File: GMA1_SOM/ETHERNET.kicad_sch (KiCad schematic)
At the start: 6 parts, among them U3 LAN8742A-CZ-TR, Y1 SG-210STF 25.0000ML0

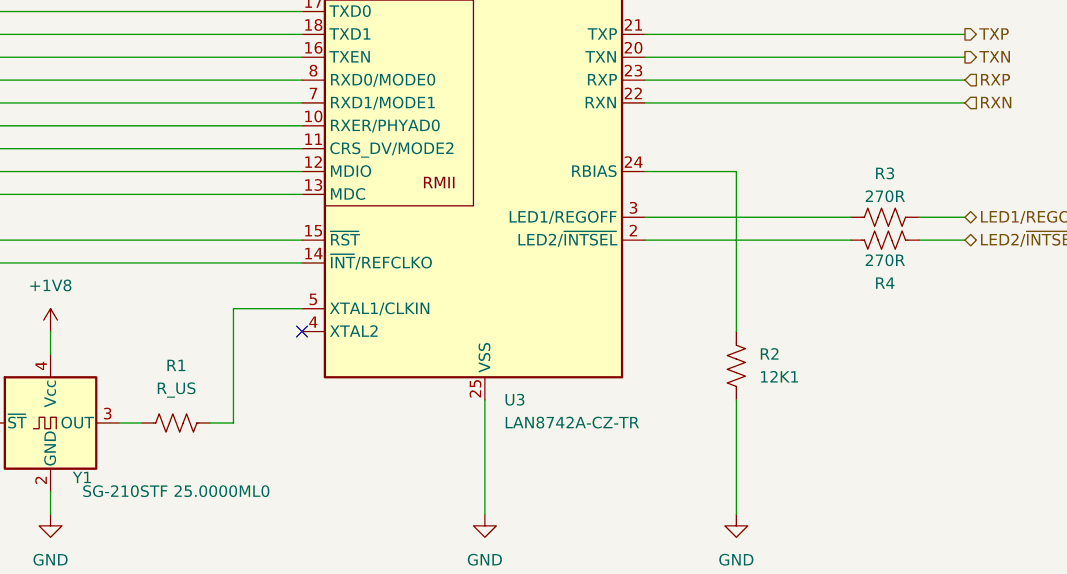
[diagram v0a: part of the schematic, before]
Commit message: add display and ram
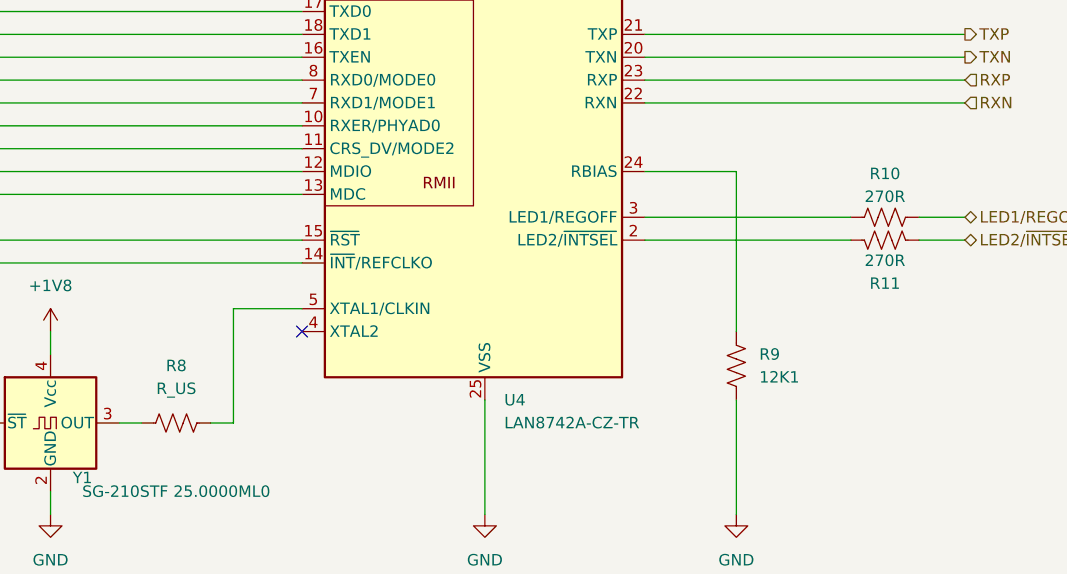
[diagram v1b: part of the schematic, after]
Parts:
- renumbered R3 to R10, R4 to R11, R1 to R8, R2 to R9, U3 to U4
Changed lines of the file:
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@@
 		(on_board yes)
 		(dnp no)
-		(property "Reference" "R3"
+		(property "Reference" "R10"
 			(at 193.04 94.234 90)
 			(effects
@@
 			(project "GMA1_SOM"
 				(path "/d784c6f3-1f62-4397-857c-3a97e2a0cbd1/9d08b115-8d2a-4cae-b926-cec128a135e3/42807cf7-1018-4a17-8e91-245329e48274"
-					(reference "R3")
-					(unit 1)
-				)
-				(path "/d784c6f3-1f62-4397-857c-3a97e2a0cbd1/9d08b115-8d2a-4cae-b926-cec128a135e3/7528c9fa-157b-4a38-85d4-57bc56cff310"
-					(reference "R7")
+					(reference "R10")
+					(unit 1)
+				)
+				(path "/d784c6f3-1f62-4397-857c-3a97e2a0cbd1/9d08b115-8d2a-4cae-b926-cec128a135e3/7528c9fa-157b-4a38-85d4-57bc56cff310"
+					(reference "R14")
 					(unit 1)
 				)
@@
 		(dnp no)
 		(fields_autoplaced yes)
-		(property "Reference" "#PWR05"
+		(property "Reference" "#PWR018"
 			(at 146.05 45.72 0)
 			(effects
@@
 			(project ""
 				(path "/d784c6f3-1f62-4397-857c-3a97e2a0cbd1/9d08b115-8d2a-4cae-b926-cec128a135e3/42807cf7-1018-4a17-8e91-245329e48274"
-					(reference "#PWR05")
-					(unit 1)
-				)
-				(path "/d784c6f3-1f62-4397-857c-3a97e2a0cbd1/9d08b115-8d2a-4cae-b926-cec128a135e3/7528c9fa-157b-4a38-85d4-57bc56cff310"
-					(reference "#PWR013")
+					(reference "#PWR018")
+					(unit 1)
+				)
+				(path "/d784c6f3-1f62-4397-857c-3a97e2a0cbd1/9d08b115-8d2a-4cae-b926-cec128a135e3/7528c9fa-157b-4a38-85d4-57bc56cff310"
+					(reference "#PWR026")
 					(unit 1)
 				)
@@
 		(dnp no)
 		(fields_autoplaced yes)
-		(property "Reference" "#PWR04"
+		(property "Reference" "#PWR017"
 			(at 143.51 39.37 0)
 			(effects
@@
 			(project ""
 				(path "/d784c6f3-1f62-4397-857c-3a97e2a0cbd1/9d08b115-8d2a-4cae-b926-cec128a135e3/42807cf7-1018-4a17-8e91-245329e48274"
-					(reference "#PWR04")
-					(unit 1)
-				)
-				(path "/d784c6f3-1f62-4397-857c-3a97e2a0cbd1/9d08b115-8d2a-4cae-b926-cec128a135e3/7528c9fa-157b-4a38-85d4-57bc56cff310"
-					(reference "#PWR012")
+					(reference "#PWR017")
+					(unit 1)
+				)
+				(path "/d784c6f3-1f62-4397-857c-3a97e2a0cbd1/9d08b115-8d2a-4cae-b926-cec128a135e3/7528c9fa-157b-4a38-85d4-57bc56cff310"
+					(reference "#PWR025")
 					(unit 1)
 				)
@@
 		(dnp no)
 		(fields_autoplaced yes)
-		(property "Reference" "#PWR01"
+		(property "Reference" "#PWR014"
 			(at 88.9 115.57 0)
 			(effects
@@
 			(project "GMA1_SOM"
 				(path "/d784c6f3-1f62-4397-857c-3a97e2a0cbd1/9d08b115-8d2a-4cae-b926-cec128a135e3/42807cf7-1018-4a17-8e91-245329e48274"
-					(reference "#PWR01")
-					(unit 1)
-				)
-				(path "/d784c6f3-1f62-4397-857c-3a97e2a0cbd1/9d08b115-8d2a-4cae-b926-cec128a135e3/7528c9fa-157b-4a38-85d4-57bc56cff310"
-					(reference "#PWR09")
+					(reference "#PWR014")
+					(unit 1)
+				)
+				(path "/d784c6f3-1f62-4397-857c-3a97e2a0cbd1/9d08b115-8d2a-4cae-b926-cec128a135e3/7528c9fa-157b-4a38-85d4-57bc56cff310"
+					(reference "#PWR022")
 					(unit 1)
 				)
@@
 		(dnp no)
 		(fields_autoplaced yes)
-		(property "Reference" "#PWR03"
+		(property "Reference" "#PWR016"
 			(at 100.33 138.43 0)
 			(effects
@@
 			(project "GMA1_SOM"
 				(path "/d784c6f3-1f62-4397-857c-3a97e2a0cbd1/9d08b115-8d2a-4cae-b926-cec128a135e3/42807cf7-1018-4a17-8e91-245329e48274"
-					(reference "#PWR03")
-					(unit 1)
-				)
-				(path "/d784c6f3-1f62-4397-857c-3a97e2a0cbd1/9d08b115-8d2a-4cae-b926-cec128a135e3/7528c9fa-157b-4a38-85d4-57bc56cff310"
-					(reference "#PWR011")
+					(reference "#PWR016")
+					(unit 1)
+				)
+				(path "/d784c6f3-1f62-4397-857c-3a97e2a0cbd1/9d08b115-8d2a-4cae-b926-cec128a135e3/7528c9fa-157b-4a38-85d4-57bc56cff310"
+					(reference "#PWR024")
 					(unit 1)
 				)
@@
 		(dnp no)
 		(fields_autoplaced yes)
-		(property "Reference" "R2"
+		(property "Reference" "R9"
 			(at 179.07 114.2999 0)
 			(effects
@@
 			(project "GMA1_SOM"
 				(path "/d784c6f3-1f62-4397-857c-3a97e2a0cbd1/9d08b115-8d2a-4cae-b926-cec128a135e3/42807cf7-1018-4a17-8e91-245329e48274"
-					(reference "R2")
-					(unit 1)
-				)
-				(path "/d784c6f3-1f62-4397-857c-3a97e2a0cbd1/9d08b115-8d2a-4cae-b926-cec128a135e3/7528c9fa-157b-4a38-85d4-57bc56cff310"
-					(reference "R6")
+					(reference "R9")
+					(unit 1)
+				)
+				(path "/d784c6f3-1f62-4397-857c-3a97e2a0cbd1/9d08b115-8d2a-4cae-b926-cec128a135e3/7528c9fa-157b-4a38-85d4-57bc56cff310"
+					(reference "R13")
 					(unit 1)
 				)
@@
 		(dnp no)
 		(fields_autoplaced yes)
-		(property "Reference" "#PWR06"
+		(property "Reference" "#PWR019"
 			(at 148.59 138.43 0)
 			(effects
@@
 			(project ""
 				(path "/d784c6f3-1f62-4397-857c-3a97e2a0cbd1/9d08b115-8d2a-4cae-b926-cec128a135e3/42807cf7-1018-4a17-8e91-245329e48274"
-					(reference "#PWR06")
-					(unit 1)
-				)
-				(path "/d784c6f3-1f62-4397-857c-3a97e2a0cbd1/9d08b115-8d2a-4cae-b926-cec128a135e3/7528c9fa-157b-4a38-85d4-57bc56cff310"
-					(reference "#PWR014")
+					(reference "#PWR019")
+					(unit 1)
+				)
+				(path "/d784c6f3-1f62-4397-857c-3a97e2a0cbd1/9d08b115-8d2a-4cae-b926-cec128a135e3/7528c9fa-157b-4a38-85d4-57bc56cff310"
+					(reference "#PWR027")
 					(unit 1)
 				)
@@
 		(dnp no)
 		(fields_autoplaced yes)
-		(property "Reference" "R1"
+		(property "Reference" "R8"
 			(at 114.3 115.57 90)
 			(effects
@@
 			(project ""
 				(path "/d784c6f3-1f62-4397-857c-3a97e2a0cbd1/9d08b115-8d2a-4cae-b926-cec128a135e3/42807cf7-1018-4a17-8e91-245329e48274"
-					(reference "R1")
-					(unit 1)
-				)
-				(path "/d784c6f3-1f62-4397-857c-3a97e2a0cbd1/9d08b115-8d2a-4cae-b926-cec128a135e3/7528c9fa-157b-4a38-85d4-57bc56cff310"
-					(reference "R5")
+					(reference "R8")
+					(unit 1)
+				)
+				(path "/d784c6f3-1f62-4397-857c-3a97e2a0cbd1/9d08b115-8d2a-4cae-b926-cec128a135e3/7528c9fa-157b-4a38-85d4-57bc56cff310"
+					(reference "R12")
 					(unit 1)
 				)
@@
 		(dnp no)
 		(fields_autoplaced yes)
-		(property "Reference" "#PWR08"
+		(property "Reference" "#PWR021"
 			(at 176.53 138.43 0)
 			(effects
@@
 			(project "GMA1_SOM"
 				(path "/d784c6f3-1f62-4397-857c-3a97e2a0cbd1/9d08b115-8d2a-4cae-b926-cec128a135e3/42807cf7-1018-4a17-8e91-245329e48274"
-					(reference "#PWR08")
-					(unit 1)
-				)
-				(path "/d784c6f3-1f62-4397-857c-3a97e2a0cbd1/9d08b115-8d2a-4cae-b926-cec128a135e3/7528c9fa-157b-4a38-85d4-57bc56cff310"
-					(reference "#PWR016")
+					(reference "#PWR021")
+					(unit 1)
+				)
+				(path "/d784c6f3-1f62-4397-857c-3a97e2a0cbd1/9d08b115-8d2a-4cae-b926-cec128a135e3/7528c9fa-157b-4a38-85d4-57bc56cff310"
+					(reference "#PWR029")
 					(unit 1)
 				)
@@
 		(dnp no)
 		(fields_autoplaced yes)
-		(property "Reference" "#PWR07"
+		(property "Reference" "#PWR020"
 			(at 153.67 39.37 0)
 			(effects
@@
 			(project ""
 				(path "/d784c6f3-1f62-4397-857c-3a97e2a0cbd1/9d08b115-8d2a-4cae-b926-cec128a135e3/42807cf7-1018-4a17-8e91-245329e48274"
-					(reference "#PWR07")
-					(unit 1)
-				)
-				(path "/d784c6f3-1f62-4397-857c-3a97e2a0cbd1/9d08b115-8d2a-4cae-b926-cec128a135e3/7528c9fa-157b-4a38-85d4-57bc56cff310"
-					(reference "#PWR015")
+					(reference "#PWR020")
+					(unit 1)
+				)
+				(path "/d784c6f3-1f62-4397-857c-3a97e2a0cbd1/9d08b115-8d2a-4cae-b926-cec128a135e3/7528c9fa-157b-4a38-85d4-57bc56cff310"
+					(reference "#PWR028")
 					(unit 1)
 				)
@@
 		(dnp no)
 		(fields_autoplaced yes)
-		(property "Reference" "U3"
+		(property "Reference" "U4"
 			(at 150.7333 119.38 0)
 			(effects
@@
 			(project ""
 				(path "/d784c6f3-1f62-4397-857c-3a97e2a0cbd1/9d08b115-8d2a-4cae-b926-cec128a135e3/42807cf7-1018-4a17-8e91-245329e48274"
-					(reference "U3")
-					(unit 1)
-				)
-				(path "/d784c6f3-1f62-4397-857c-3a97e2a0cbd1/9d08b115-8d2a-4cae-b926-cec128a135e3/7528c9fa-157b-4a38-85d4-57bc56cff310"
 					(reference "U4")
+					(unit 1)
+				)
+				(path "/d784c6f3-1f62-4397-857c-3a97e2a0cbd1/9d08b115-8d2a-4cae-b926-cec128a135e3/7528c9fa-157b-4a38-85d4-57bc56cff310"
+					(reference "U5")
 					(unit 1)
 				)
@@
 		(on_board yes)
 		(dnp no)
-		(property "Reference" "R4"
+		(property "Reference" "R11"
 			(at 193.04 106.426 90)
 			(effects
@@
 			(project "GMA1_SOM"
 				(path "/d784c6f3-1f62-4397-857c-3a97e2a0cbd1/9d08b115-8d2a-4cae-b926-cec128a135e3/42807cf7-1018-4a17-8e91-245329e48274"
-					(reference "R4")
-					(unit 1)
-				)
-				(path "/d784c6f3-1f62-4397-857c-3a97e2a0cbd1/9d08b115-8d2a-4cae-b926-cec128a135e3/7528c9fa-157b-4a38-85d4-57bc56cff310"
-					(reference "R8")
+					(reference "R11")
+					(unit 1)
+				)
+				(path "/d784c6f3-1f62-4397-857c-3a97e2a0cbd1/9d08b115-8d2a-4cae-b926-cec128a135e3/7528c9fa-157b-4a38-85d4-57bc56cff310"
+					(reference "R15")
 					(unit 1)
 				)
@@
 		(dnp no)
 		(fields_autoplaced yes)
-		(property "Reference" "#PWR02"
+		(property "Reference" "#PWR015"
 			(at 100.33 115.57 0)
 			(effects
@@
 			(project "GMA1_SOM"
 				(path "/d784c6f3-1f62-4397-857c-3a97e2a0cbd1/9d08b115-8d2a-4cae-b926-cec128a135e3/42807cf7-1018-4a17-8e91-245329e48274"
-					(reference "#PWR02")
-					(unit 1)
-				)
-				(path "/d784c6f3-1f62-4397-857c-3a97e2a0cbd1/9d08b115-8d2a-4cae-b926-cec128a135e3/7528c9fa-157b-4a38-85d4-57bc56cff310"
-					(reference "#PWR010")
-					(unit 1)
-				)
+					(reference "#PWR015")
+					(unit 1)
+				)
+				(path "/d784c6f3-1f62-4397-857c-3a97e2a0cbd1/9d08b115-8d2a-4cae-b926-cec128a135e3/7528c9fa-157b-4a38-85d4-57bc56cff310"
+					(reference "#PWR023")
+					(unit 1)
+				)
